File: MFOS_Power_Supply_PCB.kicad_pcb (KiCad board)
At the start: 2 copper layers, 110 x 40.9 mm, 29 parts, among them J1 9VAC~, J2 9VAC~, J3 GND, J4 +5VDC, J5 -5VDC, M1 MountingHole_3.2mm_M3_DIN965_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, M2 MountingHole_3.2mm_M3_DIN965_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, M3 MountingHole_3.2mm_M3_DIN965_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, M4 MountingHole_3.2mm_M3_DIN965_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, U1 LM7805_TO220, U2 LM7905_TO220

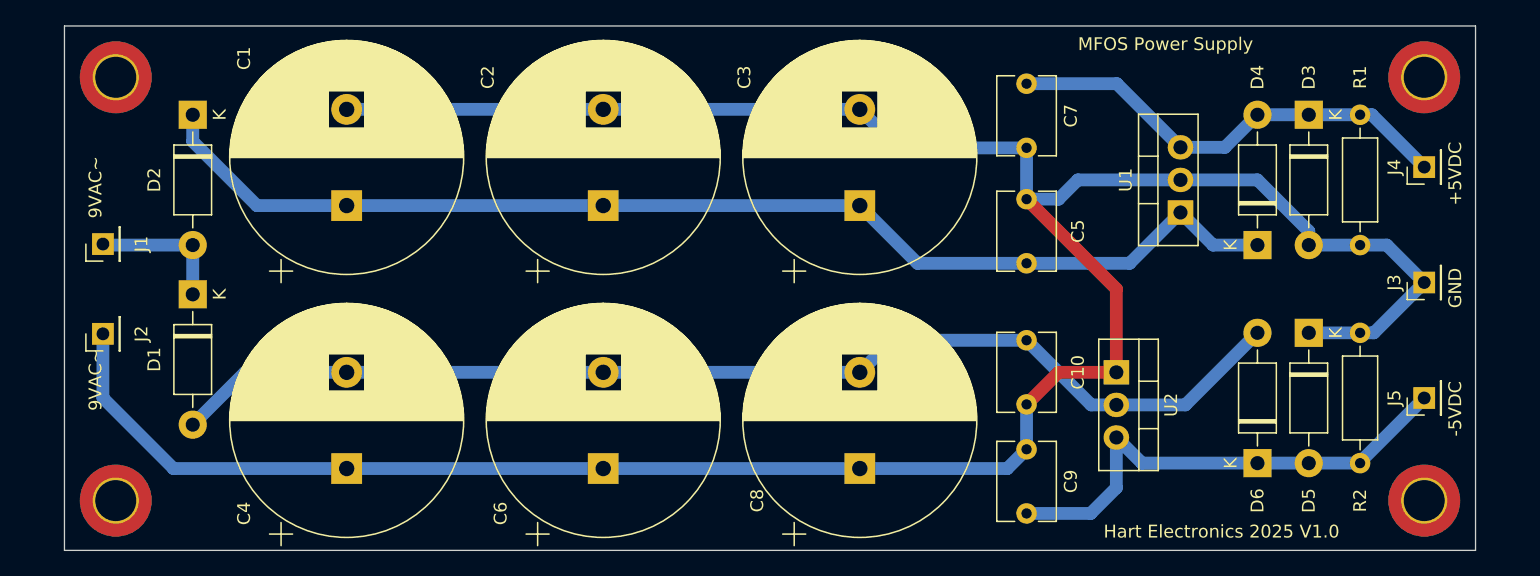
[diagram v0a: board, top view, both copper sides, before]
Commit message: increased size of pads to aid soldering V1.0 for fabrication
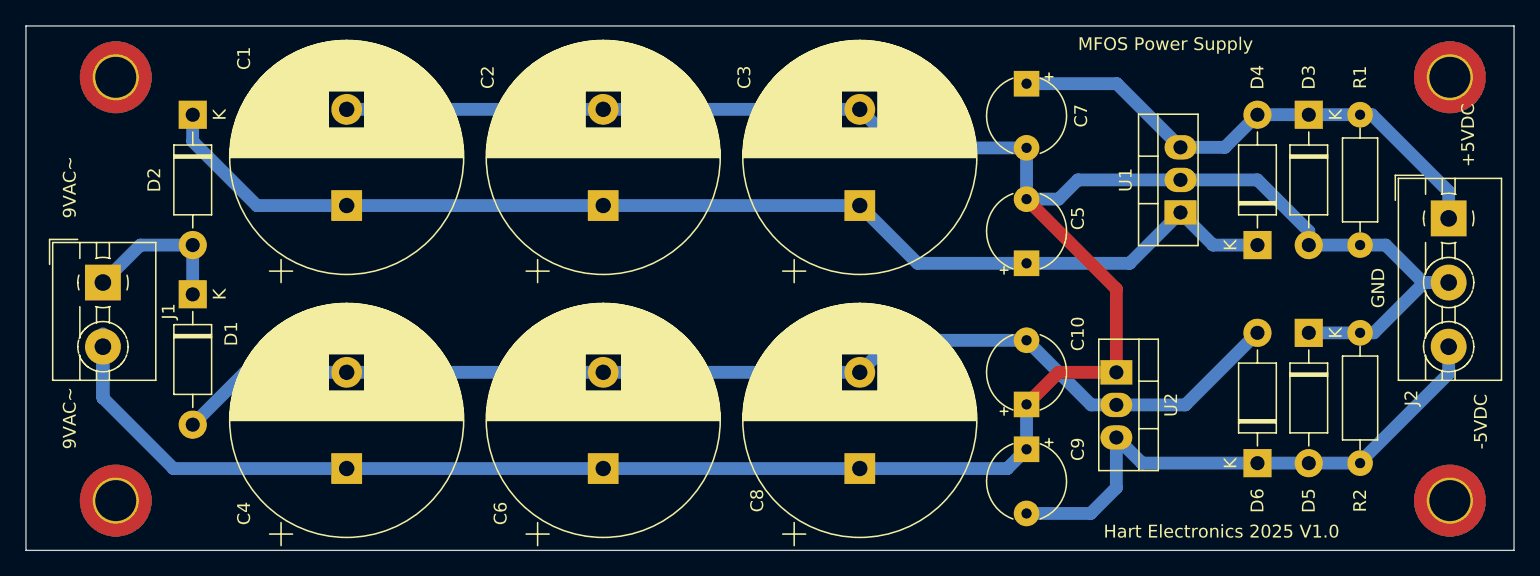
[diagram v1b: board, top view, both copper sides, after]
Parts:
- removed J3: GND, Connector_PinHeader_2.54mm:PinHeader_1x01_P2.54mm_Vertical
- removed J4: +5VDC, Connector_PinHeader_2.54mm:PinHeader_1x01_P2.54mm_Vertical
- removed J5: -5VDC, Connector_PinHeader_2.54mm:PinHeader_1x01_P2.54mm_Vertical
- C10, C5, C7, C9: footprint Capacitor_THT:C_Disc_D6.0mm_W4.4mm_P5.00mm -> Capacitor_THT:CP_Radial_Tantal_D6.0mm_P5.00mm
- J1: value 9VAC~ -> 9VAC~ IN; footprint Connector_PinHeader_2.54mm:PinHeader_1x01_P2.54mm_Vertical -> TerminalBlock:TerminalBlock_MaiXu_MX126-5.0-02P_1x02_P5.00mm
- J2: value 9VAC~ -> +/- 5VDC OUT; footprint Connector_PinHeader_2.54mm:PinHeader_1x01_P2.54mm_Vertical -> TerminalBlock:TerminalBlock_MaiXu_MX126-5.0-03P_1x03_P5.00mm
- moved J2 105.3 mm to (196.9, 87.0), turned to -90 degrees
- moved J1 3.00 mm to (92.0, 92.0), turned to -90 degrees
- moved M3 2.00 mm to (197.0, 76.0)
- moved M4 2.00 mm to (197.0, 109.0)
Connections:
- J2 pad 1: Earth -> Net-(D3-K)
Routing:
- net Earth: track 212.3 -> 219.2 mm
- net Net-(D5-A): track 38.7 -> 43.5 mm
- net Net-(D3-K): track 35.8 -> 40.6 mm
- net Net-(D1-K): track 10.9 -> 12.0 mm
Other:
- board size 110 x 40.9 mm -> 116 x 40.9 mm

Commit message: As built v1.0 Calculated actual required rating of load resistors but did not permanently install.
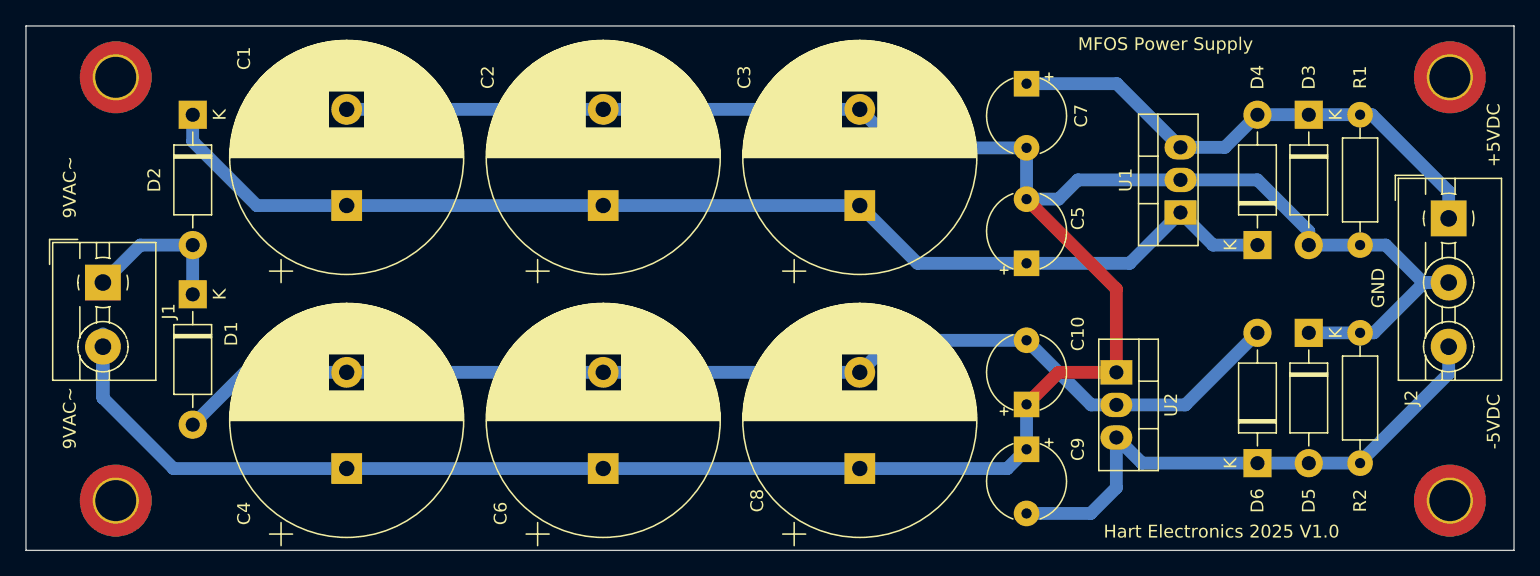
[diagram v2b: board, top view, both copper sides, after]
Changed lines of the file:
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@@
 		(fp_arc
 			(start 5.000479 1.960685)
-			(mid 4.744554 1.943974)
+			(mid 4.744554 1.943973)
 			(end 4.493 1.894)
 			(stroke
@@
 		(fp_arc
 			(start 5.829295 1.77705)
-			(mid 5.735154 1.818015)
+			(mid 5.735155 1.818016)
 			(end 5.639 1.854)
 			(stroke
@@
 		(fp_arc
 			(start 4.080344 1.730739)
-			(mid 4.005725 1.688977)
+			(mid 4.005725 1.688978)
 			(end 3.933 1.644)
 			(stroke
@@
 		(fp_arc
 			(start 6.233457 1.523294)
-			(mid 6.165839 1.575648)
+			(mid 6.16584 1.575649)
 			(end 6.096 1.625)
 			(stroke
@@
 		(fp_arc
 			(start 6.36213 1.410651)
-			(mid 6.299301 1.468722)
+			(mid 6.2993 1.468721)
 			(end 6.234 1.524)
 			(stroke
@@
 		(fp_arc
 			(start 3.521125 1.286294)
-			(mid 3.477135 1.233898)
+			(mid 3.477135 1.233899)
 			(end 3.435 1.18)
 			(stroke
@@
 		(fp_arc
 			(start 6.566102 1.179628)
-			(mid 6.523978 1.233565)
+			(mid 6.523978 1.233564)
 			(end 6.48 1.286)
 			(stroke
@@
 		(fp_arc
 			(start 3.521202 -1.287012)
-			(mid 3.578748 -1.350292)
+			(mid 3.578747 -1.350293)
 			(end 3.639 -1.411)
 			(stroke
@@
 		(fp_arc
 			(start 6.096479 -1.625751)
-			(mid 6.166349 -1.576376)
+			(mid 6.166348 -1.576374)
 			(end 6.234 -1.524)
 			(stroke
@@
 		(fp_arc
 			(start 3.93363 -1.644317)
-			(mid 4.00637 -1.689264)
+			(mid 4.006369 -1.689267)
 			(end 4.081 -1.731)
 			(stroke
@@
 		(fp_arc
 			(start 5.920652 -1.730826)
-			(mid 5.995273 -1.68902)
+			(mid 5.995274 -1.689022)
 			(end 6.068 -1.644)
 			(stroke
@@
 		(fp_arc
 			(start 5.638712 -1.85392)
-			(mid 5.734863 -1.817952)
+			(mid 5.734863 -1.817951)
 			(end 5.829 -1.777)
 			(stroke
@@
 		(fp_arc
 			(start 5.000479 1.960685)
-			(mid 4.744554 1.943974)
+			(mid 4.744554 1.943973)
 			(end 4.493 1.894)
 			(stroke
@@
 		(fp_arc
 			(start 10.000479 1.960685)
-			(mid 9.744554 1.943974)
+			(mid 9.744554 1.943973)
 			(end 9.493 1.894)
 			(stroke
@@
 		(fp_arc
 			(start 5.829295 1.77705)
-			(mid 5.735154 1.818015)
+			(mid 5.735155 1.818016)
 			(end 5.639 1.854)
 			(stroke
@@
 		(fp_arc
 			(start 10.829295 1.77705)
-			(mid 10.735154 1.818015)
+			(mid 10.735155 1.818016)
 			(end 10.639 1.854)
 			(stroke
@@
 		(fp_arc
 			(start 4.080344 1.730739)
-			(mid 4.005725 1.688977)
+			(mid 4.005725 1.688978)
 			(end 3.933 1.644)
 			(stroke
@@
 		(fp_arc
 			(start 9.080344 1.730739)
-			(mid 9.005725 1.688977)
+			(mid 9.005725 1.688978)
 			(end 8.933 1.644)
 			(stroke
@@
 		(fp_arc
 			(start 6.233457 1.523294)
-			(mid 6.165839 1.575648)
+			(mid 6.16584 1.575649)
 			(end 6.096 1.625)
 			(stroke
@@
 		(fp_arc
 			(start 11.233457 1.523294)
-			(mid 11.165839 1.575648)
+			(mid 11.16584 1.575649)
 			(end 11.096 1.625)
 			(stroke
@@
 		(fp_arc
 			(start 6.36213 1.410651)
-			(mid 6.299301 1.468722)
+			(mid 6.2993 1.468721)
 			(end 6.234 1.524)
 			(stroke
@@
 		(fp_arc
 			(start 11.36213 1.410651)
-			(mid 11.299301 1.468722)
+			(mid 11.2993 1.468721)
 			(end 11.234 1.524)
 			(stroke
@@
 		(fp_arc
 			(start 3.521125 1.286294)
-			(mid 3.477135 1.233898)
+			(mid 3.477135 1.233899)
 			(end 3.435 1.18)
 			(stroke
@@
 		(fp_arc
 			(start 8.521125 1.286294)
-			(mid 8.477135 1.233898)
+			(mid 8.477135 1.233899)
 			(end 8.435 1.18)
 			(stroke
@@
 		(fp_arc
 			(start 6.566102 1.179628)
-			(mid 6.523978 1.233565)
+			(mid 6.523978 1.233564)
 			(end 6.48 1.286)
 			(stroke
@@
 		(fp_arc
 			(start 11.566102 1.179628)
-			(mid 11.523978 1.233565)
+			(mid 11.523978 1.233564)
 			(end 11.48 1.286)
 			(stroke
@@
 		(fp_arc
 			(start 3.521202 -1.287012)
-			(mid 3.578748 -1.350292)
+			(mid 3.578747 -1.350293)
 			(end 3.639 -1.411)
 			(stroke
@@
 		(fp_arc
 			(start 8.521202 -1.287012)
-			(mid 8.578748 -1.350292)
+			(mid 8.578747 -1.350293)
 			(end 8.639 -1.411)
 			(stroke
@@
 		(fp_arc
 			(start 6.096479 -1.625751)
-			(mid 6.166349 -1.576376)
+			(mid 6.166348 -1.576374)
 			(end 6.234 -1.524)
 			(stroke
@@
 		(fp_arc
 			(start 11.096479 -1.625751)
-			(mid 11.166349 -1.576376)
+			(mid 11.166348 -1.576374)
 			(end 11.234 -1.524)
 			(stroke
@@
 		(fp_arc
 			(start 3.93363 -1.644317)
-			(mid 4.00637 -1.689264)
+			(mid 4.006369 -1.689267)
 			(end 4.081 -1.731)
 			(stroke
@@
 		(fp_arc
 			(start 8.93363 -1.644317)
-			(mid 9.00637 -1.689264)
+			(mid 9.006369 -1.689267)
 			(end 9.081 -1.731)
 			(stroke
@@
 		(fp_arc
 			(start 5.920652 -1.730826)
-			(mid 5.995273 -1.68902)
+			(mid 5.995274 -1.689022)
 			(end 6.068 -1.644)
 			(stroke
@@
 		(fp_arc
 			(start 10.920652 -1.730826)
-			(mid 10.995273 -1.68902)
+			(mid 10.995274 -1.689022)
 			(end 11.068 -1.644)
 			(stroke
@@
 		(fp_arc
 			(start 5.638712 -1.85392)
-			(mid 5.734863 -1.817952)
+			(mid 5.734863 -1.817951)
 			(end 5.829 -1.777)
 			(stroke
@@
 		(fp_arc
 			(start 10.638712 -1.85392)
-			(mid 10.734863 -1.817952)
+			(mid 10.734863 -1.817951)
 			(end 10.829 -1.777)
 			(stroke
@@
 	)
 	(gr_text "-5VDC"
-		(at 200 105 90)
+		(at 201 105 90)
 		(layer "F.SilkS")
 		(effects
@@
 	)
 	(gr_text "+5VDC"
-		(at 199 83 90)
+		(at 201 83 90)
 		(layer "F.SilkS")
 		(effects
